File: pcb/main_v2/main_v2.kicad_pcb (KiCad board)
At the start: 4 copper layers, 68.5 x 135.2 mm, 97 parts, among them IC201 AP22811AW5-7, IC301 SE2576L-R, IC302 RMS-30+, IC401 RMS-30+, IC402 HMC374, IC501 SPF5043Z, IC502 PD0922J5050S2HF, IC503 SPF5043Z, J102 Conn_02x06_Odd_Even, J201 USB_A, J301 Conn_Coaxial, J302 Conn_Coaxial, J401 Conn_Coaxial, J402 Conn_Coaxial, SW201 SW_DIP_x01, U201 LT3042xMSE, U501 XMB0220K1-50100G, Y501 ASGTX-P-1.500GHZ-1

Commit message: updarted schematic and simulation
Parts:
- removed C504: 100 pF, Capacitor_SMD:C_0402_1005Metric
- removed C505, C509: 0.1 uF, Capacitor_SMD:C_0603_1608Metric
- removed C506, C507, C508, C510, C511, C512: 100 pF, Capacitor_SMD:C_0603_1608Metric
- removed FL501: LFCN-1700D+, My Footprints:LFCN1700D
- removed IC501, IC503: SPF5043Z, My Footprints:SPF5043Z
- removed IC502: PD0922J5050S2HF, My Footprints:PD0922J5050S2HF
- removed J102: Conn_02x06_Odd_Even, Connector_PinHeader_2.54mm:PinHeader_2x06_P2.54mm_Vertical
- removed L501, L502: 27 nH, Inductor_SMD:L_0603_1608Metric
- removed R501: 10, Resistor_SMD:R_0402_1005Metric
- removed R502, R503: 150 R, Resistor_SMD:R_0603_1608Metric
- removed R504, R505: DNI, Resistor_SMD:R_0603_1608Metric
- removed U501: XMB0220K1-50100G, My Footprints:XMB0220K1-50100G_TTT
- removed Y501: ASGTX-P-1.500GHZ-1, My Footprints:ASGTX
- added C408: 150 pF, Capacitor_SMD:C_0402_1005Metric, F.Cu at (179.9, 148.6)
- added C601: 0.1 uF, Capacitor_SMD:C_0402_1005Metric, F.Cu at (192.0, 124.0)
- added C602: 10 pF, Capacitor_SMD:C_0402_1005Metric, F.Cu at (192.0, 126.0)
- added C603: 0.1 uF, Capacitor_SMD:C_0402_1005Metric, F.Cu at (192.0, 127.9)
- added C604: 10 pF, Capacitor_SMD:C_0402_1005Metric, F.Cu at (192.0, 129.9)
- added C605: 2.7 nF, Capacitor_SMD:C_0402_1005Metric, F.Cu at (192.0, 131.9)
- added C606: 1.2 nF, Capacitor_SMD:C_0402_1005Metric, F.Cu at (192.0, 133.8)
- added C607: 39 nF, Capacitor_SMD:C_0402_1005Metric, F.Cu at (192.0, 135.8)
- added C608: 10 pF, Capacitor_SMD:C_0402_1005Metric, F.Cu at (194.8, 124.0)
- added C609: 0.1 uF, Capacitor_SMD:C_0402_1005Metric, F.Cu at (194.8, 126.0)
- added C610: 0.1 uF, Capacitor_SMD:C_0402_1005Metric, F.Cu at (194.8, 127.9)
- added C611: 120 pF, Capacitor_SMD:C_0402_1005Metric, F.Cu at (194.8, 129.9)
- added C612: 120 pF, Capacitor_SMD:C_0402_1005Metric, F.Cu at (194.8, 131.9)
- added C613: 1 nF, Capacitor_SMD:C_0402_1005Metric, F.Cu at (194.8, 133.8)
- added C614: 1 nF, Capacitor_SMD:C_0402_1005Metric, F.Cu at (194.8, 135.8)
- added C615: 10 pF, Capacitor_SMD:C_0402_1005Metric, F.Cu at (197.7, 124.0)
- added C616: 0.1 uF, Capacitor_SMD:C_0402_1005Metric, F.Cu at (197.7, 126.0)
- added C617: 10 pF, Capacitor_SMD:C_0402_1005Metric, F.Cu at (197.7, 127.9)
- added C618: 0.1 uF, Capacitor_SMD:C_0402_1005Metric, F.Cu at (197.7, 129.9)
- added C619: 10 pF, Capacitor_SMD:C_0402_1005Metric, F.Cu at (197.7, 131.9)
- added C620: 10 pF, Capacitor_SMD:C_0402_1005Metric, F.Cu at (197.7, 133.8)
- added C621: 0.1 uF, Capacitor_SMD:C_0402_1005Metric, F.Cu at (197.7, 135.8)
- added C622: 10 pF, Capacitor_SMD:C_0402_1005Metric, F.Cu at (200.6, 124.0)
- added C623: 0.1 uF, Capacitor_SMD:C_0402_1005Metric, F.Cu at (200.6, 126.0)
- added C624: 1 pF, Capacitor_SMD:C_0402_1005Metric, F.Cu at (200.6, 127.9)
- added C625: 1 pF, Capacitor_SMD:C_0402_1005Metric, F.Cu at (200.6, 129.9)
- added C626: 0.1 uF, Capacitor_SMD:C_0402_1005Metric, F.Cu at (200.6, 131.9)
- added C627: DC Cut Cap, Capacitor_SMD:C_0402_1005Metric, F.Cu at (199.6, 149.1)
- added C628: 10 pF, Capacitor_SMD:C_0402_1005Metric, F.Cu at (199.6, 151.1)
- added C629: 100 pF, Capacitor_SMD:C_0402_1005Metric, F.Cu at (212.3, 134.3)
- added C630: 100 pF, Capacitor_SMD:C_0402_1005Metric, F.Cu at (212.3, 136.2)
- added C631: 10 nF, Capacitor_SMD:C_0402_1005Metric, F.Cu at (212.3, 138.2)
- added C632: 100 pF, Capacitor_SMD:C_0402_1005Metric, F.Cu at (212.3, 140.2)
- added C633: 10 nF, Capacitor_SMD:C_0402_1005Metric, F.Cu at (212.3, 142.1)
- added C634: 100 pF, Capacitor_SMD:C_0402_1005Metric, F.Cu at (212.3, 144.1)
- added D601: LED, LED_SMD:LED_0805_2012Metric, F.Cu at (187.8, 139.6)
- added FL601: LFCN-1800+, My Footprints:LFCN1800, F.Cu at (217.2, 142.2)
- added H101: MountingHole, MountingHole:MountingHole_2.2mm_M2, F.Cu at (78.0, 61.5)
- added H102: MountingHole, MountingHole:MountingHole_2.2mm_M2, F.Cu at (138.0, 61.0)
- added H103: MountingHole, MountingHole:MountingHole_2.2mm_M2, F.Cu at (77.5, 188.0)
- added H104: MountingHole, MountingHole:MountingHole_2.2mm_M2, F.Cu at (137.5, 187.5)
- added IC601: PSA4-5043+, My Footprints:PSA45043, F.Cu at (216.5, 136.4)
- added IC602: PSA4-5043+, My Footprints:PSA45043, F.Cu at (221.9, 136.4)
- added J202: Barrel_Jack, Connector_BarrelJack:BarrelJack_CUI_PJ-063AH_Horizontal_CircularHoles, F.Cu at (132.0, 114.8)
- added L601: 7.5 nH, Inductor_SMD:L_0402_1005Metric, F.Cu at (197.1, 137.8)
- added L602: 7.5 nH, Inductor_SMD:L_0402_1005Metric, F.Cu at (197.1, 139.8)
- added L603: 47 nH, Inductor_SMD:L_0402_1005Metric, F.Cu at (222.0, 140.5)
- added L605: 47 nH, Inductor_SMD:L_0402_1005Metric, F.Cu at (220.0, 127.5)
- added R601: 51, Resistor_SMD:R_0603_1608Metric, F.Cu at (180.5, 124.3)
- added R602: 4.7 k, Resistor_SMD:R_0603_1608Metric, F.Cu at (180.5, 126.8)
- added R603: 360, Resistor_SMD:R_0603_1608Metric, F.Cu at (180.5, 129.3)
- added R604: 680, Resistor_SMD:R_0603_1608Metric, F.Cu at (180.5, 131.8)
- added R605: 10k, Resistor_SMD:R_0603_1608Metric, F.Cu at (180.5, 134.3)
- added R606: 10k, Resistor_SMD:R_0603_1608Metric, F.Cu at (180.5, 136.8)
- added R607: DNI, Resistor_SMD:R_0603_1608Metric, F.Cu at (184.5, 124.3)
- added R608: 10k, Resistor_SMD:R_0603_1608Metric, F.Cu at (184.5, 126.8)
- added R609: 10k, Resistor_SMD:R_0603_1608Metric, F.Cu at (184.5, 129.3)
- added R610: 10k, Resistor_SMD:R_0603_1608Metric, F.Cu at (184.5, 131.8)
- added R611: DNI, Resistor_SMD:R_0603_1608Metric, F.Cu at (184.5, 134.3)
- added R612: 0, Resistor_SMD:R_0603_1608Metric, F.Cu at (184.5, 136.8)
- added R613: 100, Resistor_SMD:R_0603_1608Metric, F.Cu at (188.5, 124.3)
- added R614: 0, Resistor_SMD:R_0603_1608Metric, F.Cu at (188.5, 126.8)
- added R615: 0, Resistor_SMD:R_0603_1608Metric, F.Cu at (188.5, 129.3)
- added R701: 200, Resistor_SMD:R_0402_1005Metric, F.Cu at (198.1, 157.0)
- added R702: 100, Resistor_SMD:R_0402_1005Metric, F.Cu at (198.1, 159.0)
- added U601: ADF4351, Package_CSP:LFCSP-32-1EP_5x5mm_P0.5mm_EP3.25x3.25mm, F.Cu at (182.0, 141.6)
- added U602: XMB0220K1-50100G, My Footprints:XMB0220K1-50100G_TTT, F.Cu at (187.7, 143.1)
- added U701: PD0922J5050D2HF, My Footprints:PD0922J5050D2HF, F.Cu at (194.1, 158.2)
- added Y601: ATX-11-F-26.000MHZ-F05-T, My Footprints:ATX11F26000MHZF05T, F.Cu at (194.8, 151.1)
- C501: value 100 pF -> 0.1 uF
- C502: value 100 pF -> 10 pF
- C503: value 100 pF -> 120 pF
- D202, D203, D204, D205, D301: footprint LED_SMD:LED_0603_1608Metric -> LED_SMD:LED_0805_2012Metric
- moved C501 120.3 mm to (212.3, 148.1)
- moved C503 105.4 mm to (212.3, 152.0)
- moved C502 102.8 mm to (212.3, 150.1), turned to 0 degrees
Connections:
- net /receiver/Rx In renamed /receiver/f = 2.4 GHz
- net /receiver/Rx In 1 renamed Net-(FL401-IN/OUT)
- net /receiver/downconverted Rx renamed Net-(IC401-IF)
- net /receiver/downconverted Rx 1 renamed Net-(FL402-RF_IN)
- net /receiver/lo in renamed Net-(IC401-LO)
- net /receiver/low filtered Rx renamed Net-(FL402-RF_OUT)
- net /receiver/low filtered Rx 1 renamed /receiver/f_sdr = 0.9 GHz
- net /transmitter/LO in renamed Net-(IC302-LO)
- net /transmitter/Power 1 renamed Net-(IC301-VCC1)
- net /transmitter/Tx In 1 renamed Net-(IC302-IF)
- net /transmitter/Upconverted renamed Net-(IC302-RF)
- net /transmitter/Upconverted 1 renamed /transmitter/f_antenne = 2.4 GHz
- net /transmitter/amplified Tx renamed Net-(IC301-RFOUT)
- net /transmitter/amplified Tx 1 renamed Net-(C306-Pad2)
- net /transmitter/amplified Tx 2 renamed Net-(J301-In)
- net CONN-2 renamed /IO Interface/Power Faulty
- net CONN-3 renamed /IO Interface/PA Enable
- net CONN-4 renamed /IO Interface/PA DET Output
- net USB Power renamed /power/USB Power
- C312 pad 2: Carrier Frequency: Tx -> /OX Splitter/Oscillator Tx
- C403 pad 2: Carrier Frequency: Rx -> /OX Splitter/Oscillator Rx
- C404 pad 1: /receiver/amplified Rx -> Net-(IC402-OUT)
- C404 pad 2: /receiver/amplified Rx 1 -> /receiver/amplified Rx
- C501 pad 1: /oscillator/unbalanced OX DC0 -> +3.3V
- C501 pad 2: /oscillator/unbalanced OX 1 -> GND
- C502 pad 1: Net-(Y501-BY-PASS/VC) -> +3.3V
- C503 pad 1: /oscillator/TXC 0DC P -> GND
- C503 pad 2: /oscillator/TCX P -> +3.3V
- FL401 pad 4: /receiver/filtered Rx -> Net-(FL401-_IN/OUT)
- IC401 pad 4: /receiver/amplified Rx 1 -> /receiver/amplified Rx
- IC402 pad 3: /receiver/filtered Rx -> Net-(IC402-IN)
- IC402 pad 6: /receiver/amplified Rx -> Net-(IC402-OUT)
- L401 pad 2: /receiver/amplified Rx -> Net-(IC402-OUT)
- SW201 pad 1: CONN-1 -> /IO Interface/Power Enable
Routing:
- net +5V: track 279.6 -> 160.9 mm, vias 78 -> 52
- net GND: track 368.6 -> 277.3 mm, vias 180 -> 139
- net CONN-1: track 74.9 -> 0.00 mm, vias 2 -> 0
- net /IO Interface/Power Enable: track 0.00 -> 71.4 mm, vias 0 -> 1
- net +3.3V: track 81.9 -> 42.2 mm, vias 37 -> 18
- net /oscillator/TCX P: track 23.9 -> 0.00 mm
- net /oscillator/TCX N: track 20.5 -> 0.00 mm
- net /oscillator/amplified XO 1: track 15.9 -> 0.00 mm
- net Net-(Y501-BY-PASS/VC): track 11.7 -> 0.00 mm
- net /oscillator/filtered XO 1: track 11.6 -> 0.00 mm
- net Net-(IC402-OUT): track 0.00 -> 10.3 mm
- net Carrier Frequency: Tx: track 9.54 -> 0.00 mm
- net /oscillator/amplified XO 2: track 8.90 -> 0.00 mm
- net /oscillator/TXC 0DC N: track 8.54 -> 0.00 mm
- net /oscillator/TXC 0DC P: track 7.65 -> 0.00 mm
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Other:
- board text added: "TODO: - via fencing - via sticthicng with ground plane - component values on silkscreen"
- board text removed: "TODO: - via fencing - via sticthicng with ground plane"

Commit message: improved python mode
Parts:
- removed C205: 4.7 nF, Capacitor_SMD:C_1206_3216Metric
- removed J201: USB_A, Connector_USB:USB3_A_Receptacle_Wuerth_692122030100
- removed J202: Barrel_Jack, Connector_BarrelJack:BarrelJack_CUI_PJ-063AH_Horizontal_CircularHoles
- removed J301, J302, J401, J402: Conn_Coaxial, Connector_Coaxial:SMA_Amphenol_132289_EdgeMount
- removed R202: 1M, Resistor_SMD:R_0603_1608Metric
- added J101: Conn_Coaxial, Connector_Coaxial:SMA_Amphenol_132289_EdgeMount, F.Cu at (242.8, 107.6)
- added J102: Conn_Coaxial, Connector_Coaxial:SMA_Amphenol_132289_EdgeMount, F.Cu at (242.8, 119.8)
- added J103: Conn_Coaxial, Connector_Coaxial:SMA_Amphenol_132289_EdgeMount, F.Cu at (242.8, 132.0)
- added J104: Conn_Coaxial, Connector_Coaxial:SMA_Amphenol_132289_EdgeMount, F.Cu at (242.8, 144.2)
- added J105: Barrel_Jack, Connector_BarrelJack:BarrelJack_CUI_PJ-063AH_Horizontal_CircularHoles, F.Cu at (265.0, 104.5)
- added J701: Conn_01x03_Pin, Connector_PinHeader_2.54mm:PinHeader_1x03_P2.54mm_Vertical, F.Cu at (136.4, 112.3)
- C313, C314, C406, C407: value 10 pF -> 100 pF
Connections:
- net /OX Splitter/Oscillator In renamed Net-(FL601-RF_IN)
- net /OX Splitter/Oscillator Rx renamed /Oscillator Splitter/Oscillator Rx
- net /OX Splitter/Oscillator Tx renamed /Oscillator Splitter/Oscillator Tx
- net /OX Splitter/Rx renamed /Oscillator Splitter/Rx
- net /OX Splitter/Tx renamed /Oscillator Splitter/Tx
- net /oscillator/TCXO renamed /Phase locked loop/TCXO
- net /transmitter/f_antenne = 2.4 GHz renamed Net-(FL301-IN/OUT)
- net Net-(J301-In) renamed /transmitter/Tx Out
- C404 pad 1: Net-(IC402-OUT) -> Net-(IC401-RF)
- C405 pad 1: /receiver/f = 2.4 GHz -> /receiver/Rx In
- C407 pad 2: /receiver/f_sdr = 0.9 GHz -> /receiver/Rx Out
- C624 pad 2: /oscillator/OX Out + -> /Oscillator Splitter/Oscillator In +
- C625 pad 2: /oscillator/OX Out - -> /Oscillator Splitter/Oscillator In -
- C631 pad 1: unconnected-(C631-Pad1) -> GND
- C633 pad 1: unconnected-(C633-Pad1) -> GND
- FL402 pad 1: GND -> unconnected-(FL402-GROUND_1-Pad1)
- IC401 pad 4: /receiver/amplified Rx -> Net-(IC401-RF)
- IC402 pad 6: Net-(IC402-OUT) -> /receiver/amplified Rx
- L401 pad 2: Net-(IC402-OUT) -> /receiver/amplified Rx
- L601 pad 2: /oscillator/OX Out + -> /Oscillator Splitter/Oscillator In +
- L602 pad 2: /oscillator/OX Out - -> /Oscillator Splitter/Oscillator In -
- U602 pad 5: /oscillator/OX Out - -> /Oscillator Splitter/Oscillator In +
- U602 pad 6: /oscillator/OX Out + -> /Oscillator Splitter/Oscillator In -
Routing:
- net /power/Shield: track 37.8 -> 0.00 mm
- net (no net): track 7.35 -> 45.2 mm
- net /receiver/f_sdr = 0.9 GHz: track 12.6 -> 0.00 mm
- net /receiver/Rx Out: track 0.00 -> 12.6 mm
- net /receiver/f = 2.4 GHz: track 10.9 -> 0.00 mm
- net /receiver/Rx In: track 0.00 -> 10.9 mm
- net Net-(IC402-OUT): track 10.3 -> 0.00 mm
- net /receiver/amplified Rx: track 5.58 -> 15.9 mm
- net GND: track 277.3 -> 273.1 mm, vias 139 -> 137
- net unconnected-(FL402-GROUND_1-Pad1): track 0.00 -> 4.21 mm, vias 0 -> 2

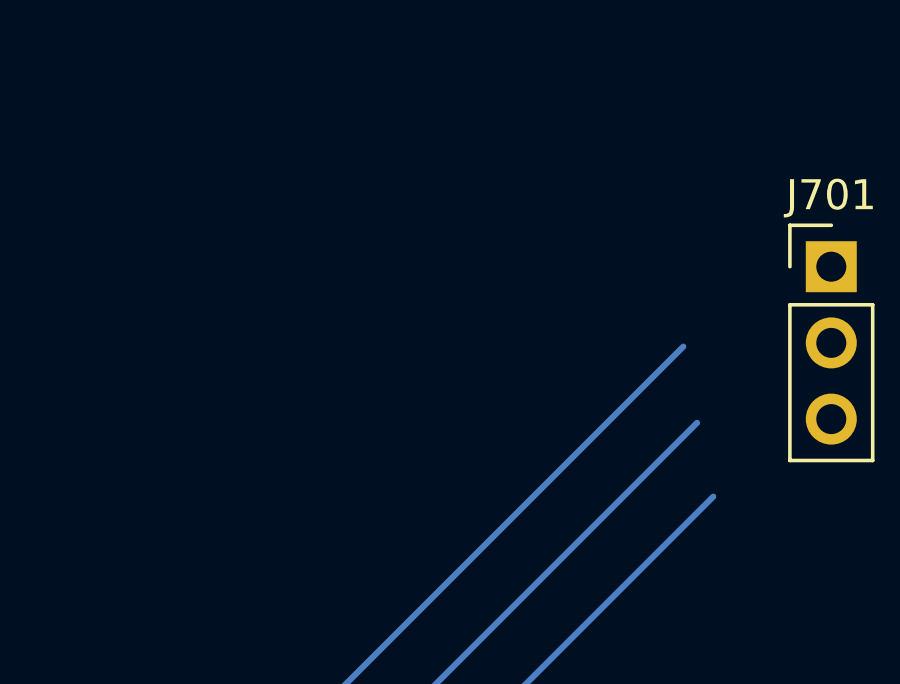
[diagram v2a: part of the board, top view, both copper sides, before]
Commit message: added noise calc for simulation
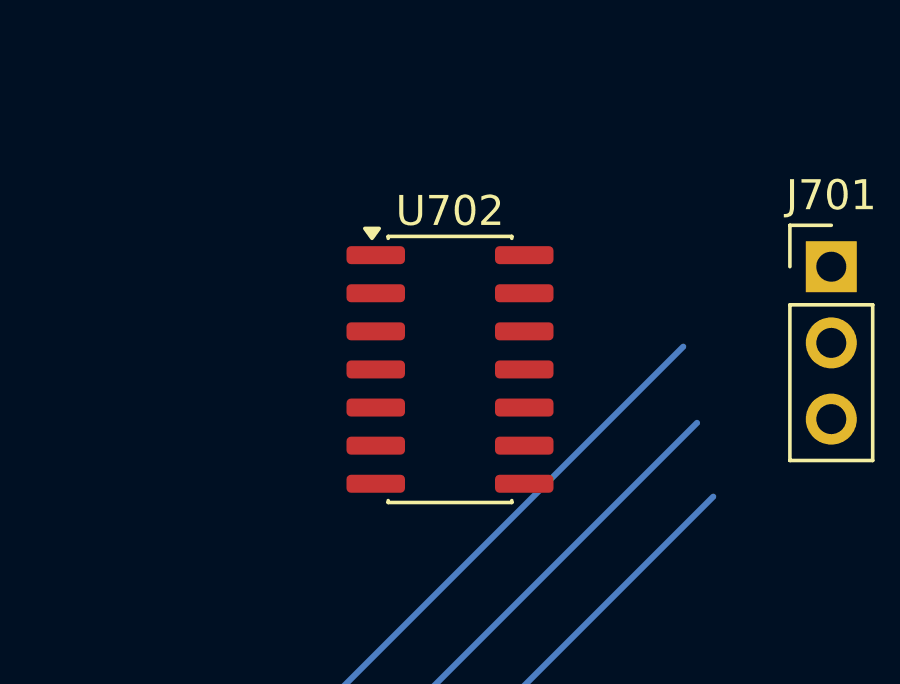
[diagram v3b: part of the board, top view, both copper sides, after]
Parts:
- added U702: TXB0104D, Package_SO:SOIC-14_3.9x8.7mm_P1.27mm, F.Cu at (123.7, 115.8)

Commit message: updated io schematic
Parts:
- removed C314, C629, C630, C632, C634: 100 pF, Capacitor_SMD:C_0402_1005Metric
- removed C607: 39 nF, Capacitor_SMD:C_0402_1005Metric
- removed C608, C615, C617, C619, C620, C622, C628: 10 pF, Capacitor_SMD:C_0402_1005Metric
- removed C609, C610, C616, C618, C621, C623, C626: 0.1 uF, Capacitor_SMD:C_0402_1005Metric
- removed C611, C612: 120 pF, Capacitor_SMD:C_0402_1005Metric
- removed C613, C614: 1 nF, Capacitor_SMD:C_0402_1005Metric
- removed C624, C625: 1 pF, Capacitor_SMD:C_0402_1005Metric
- removed C627: DC Cut Cap, Capacitor_SMD:C_0402_1005Metric
- removed C631, C633: 10 nF, Capacitor_SMD:C_0402_1005Metric
- removed D601: LED, LED_SMD:LED_0805_2012Metric
- removed L603, L605: 47 nH, Inductor_SMD:L_0402_1005Metric
- removed R206: 453 k, Resistor_SMD:R_0603_1608Metric
- removed R603: 360, Resistor_SMD:R_0603_1608Metric
- removed R604: 680, Resistor_SMD:R_0603_1608Metric
- removed R605, R606, R608, R609, R610: 10k, Resistor_SMD:R_0603_1608Metric
- removed R607, R611: DNI, Resistor_SMD:R_0603_1608Metric
- removed R612, R614, R615: 0, Resistor_SMD:R_0603_1608Metric
- removed R613: 100, Resistor_SMD:R_0603_1608Metric
- removed U701: PD0922J5050D2HF, My Footprints:PD0922J5050D2HF
- removed U702: TXB0104D, Package_SO:SOIC-14_3.9x8.7mm_P1.27mm
- removed Y601: ATX-11-F-26.000MHZ-F05-T, My Footprints:ATX11F26000MHZF05T
- added C205: 4.7 uF, Capacitor_SMD:C_0603_1608Metric, F.Cu at (382.7, 108.1)
- added C311: 10 pF, Capacitor_SMD:C_0402_1005Metric, F.Cu at (388.1, 107.8)
- added C504: 0.1 uF, Capacitor_SMD:C_0402_1005Metric, F.Cu at (382.1, 83.7)
- added C505: 10 pF, Capacitor_SMD:C_0402_1005Metric, F.Cu at (382.1, 85.7)
- added C506: 0.1 uF, Capacitor_SMD:C_0402_1005Metric, F.Cu at (382.1, 87.6)
- added C507: 10 pF, Capacitor_SMD:C_0402_1005Metric, F.Cu at (382.1, 89.6)
- added C508: 10 pF, Capacitor_SMD:C_0402_1005Metric, F.Cu at (382.1, 91.6)
- added C509: 0.1 uF, Capacitor_SMD:C_0402_1005Metric, F.Cu at (382.1, 93.5)
- added C510: 120 pF, Capacitor_SMD:C_0402_1005Metric, F.Cu at (382.1, 95.5)
- added C511: 10 pF, Capacitor_SMD:C_0402_1005Metric, F.Cu at (382.1, 97.5)
- added C512: 0.1 uF, Capacitor_SMD:C_0402_1005Metric, F.Cu at (385.0, 83.7)
- added C513: 120 pF, Capacitor_SMD:C_0402_1005Metric, F.Cu at (385.0, 85.7)
- added C514: 1 pF, Capacitor_SMD:C_0402_1005Metric, F.Cu at (385.0, 87.6)
- added C515: 1 pF, Capacitor_SMD:C_0402_1005Metric, F.Cu at (385.0, 89.6)
- added C516: 1 nF, Capacitor_SMD:C_0402_1005Metric, F.Cu at (385.0, 91.6)
- added C517: 1 nF, Capacitor_SMD:C_0402_1005Metric, F.Cu at (385.0, 93.5)
- added C518: 0.1 uF, Capacitor_SMD:C_0402_1005Metric, F.Cu at (385.0, 95.5)
- added C519: 10 pF, Capacitor_SMD:C_0402_1005Metric, F.Cu at (385.0, 97.5)
- added C520: 2.7 nF, Capacitor_SMD:C_0402_1005Metric, F.Cu at (387.9, 83.7)
- added C521: 39 nF, Capacitor_SMD:C_0402_1005Metric, F.Cu at (387.9, 85.7)
- added C522: 1.2 nF, Capacitor_SMD:C_0402_1005Metric, F.Cu at (387.9, 87.6)
- added C523: 0.1 uF, Capacitor_SMD:C_0402_1005Metric, F.Cu at (387.9, 89.6)
- added C524: 10 pF, Capacitor_SMD:C_0402_1005Metric, F.Cu at (387.9, 91.6)
- added C525: 0.1 uF, Capacitor_SMD:C_0402_1005Metric, F.Cu at (387.9, 93.5)
- added C526: 10 pF, Capacitor_SMD:C_0402_1005Metric, F.Cu at (387.9, 95.5)
- added C527: DC Cut Cap, Capacitor_SMD:C_0402_1005Metric, F.Cu at (387.9, 97.5)
- added C528: 120 pF, Capacitor_SMD:C_0402_1005Metric, F.Cu at (390.7, 83.7)
- added C529: 0.1 uF, Capacitor_SMD:C_0402_1005Metric, F.Cu at (390.7, 85.7)
- added C530: 10 pF, Capacitor_SMD:C_0402_1005Metric, F.Cu at (390.7, 87.6)
- added C531: 10 pF, Capacitor_SMD:C_0402_1005Metric, F.Cu at (390.7, 89.6)
- added C701: 0.1 uF, Capacitor_SMD:C_0402_1005Metric, F.Cu at (378.1, 55.7)
- added C702: 0.1 uF, Capacitor_SMD:C_0402_1005Metric, F.Cu at (378.1, 57.7)
- added C703: 0.1 uF, Capacitor_SMD:C_0402_1005Metric, F.Cu at (102.7, 128.7)
- added D206: LED, LED_SMD:LED_0805_2012Metric, F.Cu at (136.6, 122.3)
- added D501: LED, LED_SMD:LED_0805_2012Metric, F.Cu at (389.6, 100.0)
- added FB201: 28C0236-0JW-10, Ferrite_THT:LairdTech_28C0236-0JW-10, F.Cu at (127.3, 113.2)
- added FB202: 28C0236-0JW-10, Ferrite_THT:LairdTech_28C0236-0JW-10, F.Cu at (127.3, 122.1)
- added IC701: 74LVC244AD-Q100J, My Footprints:SOIC127P1032X265-20N, F.Cu at (107.7, 116.0)
- added IC702: LTC6992CS6-4#TRMPBF, My Footprints:SOT95P280X100-6N, F.Cu at (103.8, 125.5)
- added J702: Conn_01x01_Pin, Connector_PinHeader_2.54mm:PinHeader_1x01_P2.54mm_Vertical, F.Cu at (140.1, 70.5)
- added J703: Conn_01x03_Pin, Connector_PinHeader_2.54mm:PinHeader_1x03_P2.54mm_Vertical, F.Cu at (94.6, 79.0)
- added J704: Conn_01x03_Pin, Connector_PinHeader_2.54mm:PinHeader_1x03_P2.54mm_Vertical, F.Cu at (147.6, 70.4)
- added J705: Conn_01x01_Pin, Connector_PinHeader_2.54mm:PinHeader_1x01_P2.54mm_Vertical, F.Cu at (143.9, 70.5)
- added J706: Conn_01x01_Pin, Connector_PinHeader_2.54mm:PinHeader_1x01_P2.54mm_Vertical, F.Cu at (112.6, 78.0)
- added J707: Conn_01x01_Pin, Connector_PinHeader_2.54mm:PinHeader_1x01_P2.54mm_Vertical, F.Cu at (108.6, 78.0)
- added J709: Conn_01x03_Pin, Connector_PinHeader_2.54mm:PinHeader_1x03_P2.54mm_Vertical, F.Cu at (116.5, 123.6)
- added J710: Conn_01x03_Pin, Connector_PinHeader_2.54mm:PinHeader_1x03_P2.54mm_Vertical, F.Cu at (121.1, 123.6)
- added L501: 7.5 nH, Inductor_SMD:L_0402_1005Metric, F.Cu at (400.7, 98.8)
- added L502: 7.5 nH, Inductor_SMD:L_0402_1005Metric, F.Cu at (400.7, 100.8)
- added Q201: DMP3068L-7, My Footprints:SOT96P240X115-3N, F.Cu at (136.8, 118.6)
- added R202: 1k, Resistor_SMD:R_0603_1608Metric, F.Cu at (382.7, 110.6)
- added R212: 1k, Resistor_SMD:R_0603_1608Metric, F.Cu at (136.3, 115.0)
- added R501: 100, Resistor_SMD:R_0603_1608Metric, F.Cu at (394.2, 84.0)
- added R502: 10k, Resistor_SMD:R_0603_1608Metric, F.Cu at (394.2, 86.5)
- added R503: 10k, Resistor_SMD:R_0603_1608Metric, F.Cu at (394.2, 89.0)
- added R504: 10k, Resistor_SMD:R_0603_1608Metric, F.Cu at (394.2, 91.5)
- added R505: DNI, Resistor_SMD:R_0603_1608Metric, F.Cu at (394.2, 94.0)
- added R506: 10k, Resistor_SMD:R_0603_1608Metric, F.Cu at (394.2, 96.5)
- added R507: 0, Resistor_SMD:R_0603_1608Metric, F.Cu at (398.2, 84.0)
- added R508: 0, Resistor_SMD:R_0603_1608Metric, F.Cu at (398.2, 86.5)
- added R509: DNI, Resistor_SMD:R_0603_1608Metric, F.Cu at (398.2, 89.0)
- added R510: 0, Resistor_SMD:R_0603_1608Metric, F.Cu at (398.2, 91.5)
- added R511: 51, Resistor_SMD:R_0603_1608Metric, F.Cu at (398.2, 94.0)
- added R512: 680, Resistor_SMD:R_0603_1608Metric, F.Cu at (398.2, 96.5)
- added R513: 360, Resistor_SMD:R_0603_1608Metric, F.Cu at (402.2, 84.0)
- added R514: 4.7 k, Resistor_SMD:R_0603_1608Metric, F.Cu at (402.2, 86.5)
- added R515: 10k, Resistor_SMD:R_0603_1608Metric, F.Cu at (402.2, 89.0)
- added R703: 100R, Resistor_SMD:R_0603_1608Metric, F.Cu at (140.6, 90.2)
- added R704: 100R, Resistor_SMD:R_0603_1608Metric, F.Cu at (374.7, 58.5)
- added R705: 100R, Resistor_SMD:R_0603_1608Metric, F.Cu at (374.7, 61.0)
- added R706: 100R, Resistor_SMD:R_0603_1608Metric, F.Cu at (374.7, 63.5)
- added R707: 100R, Resistor_SMD:R_0603_1608Metric, F.Cu at (374.7, 66.0)
- added R708: 50k, Resistor_SMD:R_0603_1608Metric, F.Cu at (116.2, 110.0)
- added R709: 100R, Resistor_SMD:R_0603_1608Metric, F.Cu at (116.2, 112.5)
- added R710: 100R, Resistor_SMD:R_0603_1608Metric, F.Cu at (116.2, 115.0)
- added R711: 100R, Resistor_SMD:R_0603_1608Metric, F.Cu at (116.2, 117.5)
- added R712: 100R, Resistor_SMD:R_0603_1608Metric, F.Cu at (116.2, 120.0)
- added U501: ADF4351, Package_CSP:LFCSP-32-1EP_5x5mm_P0.5mm_EP3.25x3.25mm, F.Cu at (395.7, 101.3)
- added U703: TXB0104D, Package_SO:SOIC-14_3.9x8.7mm_P1.27mm, F.Cu at (380.2, 62.5)
- added Y501: ATX-11-F-26.000MHZ-F05-T, My Footprints:ATX11F26000MHZF05T, F.Cu at (384.0, 101.4)
- C208: value 4.7 uF -> 470u
- C312, C602: value 10 pF -> 100 pF
- C403: value 10 pF -> 150 pF
- C405: value 150 pF -> 100 pF
- C406: value 100 pF -> 10 pF
- C503: value 120 pF -> 0.1 uF
- C601: value 0.1 uF -> 10 nF
- C603: value 0.1 uF -> 100 pF
- C604: value 10 pF -> 10 nF
- C605: value 2.7 nF -> 100 pF
- C606: value 1.2 nF -> 100 pF
- IC401: value RMS-30+ -> HMC374; footprint My Footprints:RMS30 -> My Footprints:SOT95P280X145-6N
- IC402: value HMC374 -> RMS-30+; footprint My Footprints:SOT95P280X145-6N -> My Footprints:RMS30
- L601, L602: value 7.5 nH -> 47 nH
- R203: value 1k -> 10k
- R204: value 10k -> 1k
- R205: value 1k -> 453 k
- R207: value 200k -> 499
- R208: value 499 -> 49.9 k
- R209: value 49.9 k -> 150
- R210: value 150 -> 33.2k
- R211: value 33.2k -> 100k
- R601: value 51 -> 100; footprint Resistor_SMD:R_0603_1608Metric -> Resistor_SMD:R_0402_1005Metric
- R602: value 4.7 k -> 200; footprint Resistor_SMD:R_0603_1608Metric -> Resistor_SMD:R_0402_1005Metric
- R701: value 200 -> 100R; footprint Resistor_SMD:R_0402_1005Metric -> Resistor_SMD:R_0603_1608Metric
- R702: value 100 -> 100R; footprint Resistor_SMD:R_0402_1005Metric -> Resistor_SMD:R_0603_1608Metric
- U601: value ADF4351 -> PD0922J5050D2HF; footprint Package_CSP:LFCSP-32-1EP_5x5mm_P0.5mm_EP3.25x3.25mm -> My Footprints:PD0922J5050D2HF
- moved R601 271.0 mm to (451.2, 135.7), turned to -90 degrees
- moved R602 268.4 mm to (448.7, 135.7), turned to -90 degrees
- moved C601 260.6 mm to (451.5, 147.2), turned to -90 degrees
- moved R701 259.6 mm to (446.8, 82.4)
- moved R702 259.6 mm to (446.8, 84.3)
- moved C602 258.4 mm to (449.5, 147.2), turned to -90 degrees
- moved C603 256.3 mm to (447.6, 147.2), turned to -90 degrees
- moved C604 254.2 mm to (445.6, 147.2), turned to -90 degrees
- moved C605 252.1 mm to (443.6, 147.2), turned to -90 degrees
- moved U601 251.9 mm to (433.9, 137.3), turned to -90 degrees
- moved C606 250.0 mm to (441.6, 147.2), turned to -90 degrees
- moved C408 247.3 mm to (426.9, 135.2), turned to -90 degrees
- moved U602 244.7 mm to (432.3, 142.9), turned to -90 degrees
- moved L601 241.0 mm to (437.7, 152.4), turned to -90 degrees
- moved L602 238.9 mm to (435.7, 152.4), turned to -90 degrees
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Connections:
- C206 pad 1: GND -> +5V
- C206 pad 2: +3.3V -> GND
- C207 pad 1: +5V -> Net-(U201-SET)
- C208 pad 1: Net-(U201-SET) -> /power/USB Power
- C312 pad 1: Net-(IC302-LO) -> /transmitter/Tx In
- C312 pad 2: /Oscillator Splitter/Oscillator Tx -> Net-(IC302-IF)
- C313 pad 1: /transmitter/Tx In -> Net-(IC302-RF)
- C313 pad 2: Net-(IC302-IF) -> Net-(FL301-IN/OUT)
- C403 pad 1: Net-(IC401-LO) -> /receiver/Rx In
- C403 pad 2: /Oscillator Splitter/Oscillator Rx -> Net-(FL401-IN/OUT)
- C404 pad 1: Net-(IC401-RF) -> Net-(FL401-_IN/OUT)
- C404 pad 2: /receiver/amplified Rx -> Net-(IC401-IN)
- C405 pad 1: /receiver/Rx In -> Net-(FL402-RF_OUT)
- C405 pad 2: Net-(FL401-IN/OUT) -> /receiver/Rx Out
- C406 pad 1: Net-(IC401-IF) -> Net-(IC402-LO)
- C406 pad 2: Net-(FL402-RF_IN) -> /Oscillator Splitter/Oscillator Rx
- C407 pad 1: Net-(FL402-RF_OUT) -> Net-(IC402-IF)
- C407 pad 2: /receiver/Rx Out -> Net-(FL402-RF_IN)
- C408 pad 1: Net-(FL401-_IN/OUT) -> Net-(IC402-RF)
- C408 pad 2: Net-(IC402-IN) -> /receiver/amplified Rx
- C503 pad 1: GND -> +3.3V
- C503 pad 2: +3.3V -> GND
- C601 pad 1: +3.3V -> GND
- C601 pad 2: GND -> +5V
- C602 pad 1: +3.3V -> Net-(IC601-RF-OUT_&_DC-IN)
- C602 pad 2: GND -> /Oscillator Splitter/Oscillator Tx
- C603 pad 1: +3.3V -> /Oscillator Splitter/Tx
- C603 pad 2: GND -> Net-(IC601-RF_IN)
- C604 pad 1: +3.3V -> GND
- C604 pad 2: GND -> +5V
- C605 pad 1: GND -> Net-(IC602-RF-OUT_&_DC-IN)
- C605 pad 2: Net-(U601-CPout) -> /Oscillator Splitter/Oscillator Rx
- C606 pad 1: GND -> /Oscillator Splitter/Rx
- C606 pad 2: Net-(U601-VTUNE) -> Net-(IC602-RF_IN)
- D201 pad 1: /power/USB Power -> /power/DC Power
- IC201 pad 3: /IO Interface/Power Faulty -> /power/Power Faulty
- IC401 pad 1: Net-(IC401-LO) -> unconnected-(IC401-N/C_1-Pad1)
- IC401 pad 3: GND -> Net-(IC401-IN)
- IC401 pad 4: Net-(IC401-RF) -> unconnected-(IC401-N/C_2-Pad4)
- IC401 pad 5: Net-(IC401-IF) -> GND
- IC401 pad 6: GND -> /receiver/amplified Rx
- IC402 pad 1: unconnected-(IC402-N/C_1-Pad1) -> Net-(IC402-LO)
- IC402 pad 3: Net-(IC402-IN) -> GND
- IC402 pad 4: unconnected-(IC402-N/C_2-Pad4) -> Net-(IC402-RF)
- IC402 pad 5: GND -> Net-(IC402-IF)
- IC402 pad 6: /receiver/amplified Rx -> GND
- J101 pad 1: /receiver/Rx In -> /receiver/Rx Out
- J102 pad 1: /receiver/Rx Out -> /transmitter/Tx Out
- J103 pad 1: /transmitter/Tx In -> /receiver/Rx In
- J104 pad 1: /transmitter/Tx Out -> /transmitter/Tx In
- J105 pad 1: /power/USB Power -> /power/DC Power
- J701 pad 1: /IO Interface/SPI: CLK -> +3.3V
- J701 pad 2: /IO Interface/SPI: DATA -> Net-(IC701-1A0)
- J701 pad 3: /IO Interface/SPI: Load Enable -> GND
- L601 pad 1: +3.3V -> +5V
- L601 pad 2: /Oscillator Splitter/Oscillator In + -> Net-(IC601-RF-OUT_&_DC-IN)
- L602 pad 1: +3.3V -> +5V
- L602 pad 2: /Oscillator Splitter/Oscillator In - -> Net-(IC602-RF-OUT_&_DC-IN)
- R203 pad 1: Net-(D203-K) -> /power/USB Power
- R203 pad 2: GND -> /power/Power Faulty
- R204 pad 1: /power/USB Power -> Net-(D204-K)
- R204 pad 2: /IO Interface/Power Faulty -> /power/Power Faulty
- R205 pad 1: Net-(D204-K) -> Net-(U201-PGFB)
- R205 pad 2: /IO Interface/Power Faulty -> +3.3V
- R207 pad 1: +5V -> GND
- R207 pad 2: Net-(U201-PG) -> Net-(U201-ILIM)
- R208 pad 2: Net-(U201-ILIM) -> Net-(U201-PGFB)
- R209 pad 1: GND -> Net-(D205-K)
- R209 pad 2: Net-(U201-PGFB) -> GND
- R210 pad 1: Net-(D205-K) -> GND
- R210 pad 2: GND -> Net-(U201-SET)
- R211 pad 1: GND -> Net-(Q201-G)
- R211 pad 2: Net-(U201-SET) -> GND
- R601 pad 1: GND -> Net-(U601-MID_1)
- R601 pad 2: Net-(C613-Pad1) -> Net-(U601-MID_2)
- R602 pad 1: GND -> /Oscillator Splitter/Rx
- R602 pad 2: Net-(U601-RSET) -> /Oscillator Splitter/Tx
- R701 pad 1: /Oscillator Splitter/Rx -> /IO Interface/Power Enable
- R701 pad 2: /Oscillator Splitter/Tx -> Net-(IC701-1Y0)
- R702 pad 1: Net-(U701-MID_1) -> /IO Interface/PLL: Power Down
- TP201 pad 1: /power/USB Power -> /power/DC Power
- U201 pad 4: Net-(U201-PG) -> Net-(D206-K)
- U601 pad 1: /IO Interface/SPI: CLK -> /Oscillator Splitter/Tx
- U601 pad 2: /IO Interface/SPI: DATA -> Net-(FL601-RF_OUT)
- U601 pad 3: /IO Interface/SPI: Load Enable -> Net-(U601-MID_2)
- U601 pad 4: /IO Interface/PLL: Chip Enable -> Net-(U601-MID_1)
- U601 pad 5: unconnected-(U601-SW-Pad5) -> GND
- U601 pad 6: +3.3V -> /Oscillator Splitter/Rx
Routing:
- net /IO Interface/Power Faulty: track 78.9 -> 0.00 mm, vias 1 -> 0
- net /IO Interface/Power Enable: track 71.4 -> 30.1 mm
- net (no net): track 45.2 -> 20.5 mm, vias 0 -> 5
- net /power/Power Faulty: track 0.00 -> 23.5 mm, vias 0 -> 3
- net /IO Interface/PA Enable: track 48.6 -> 32.6 mm
- net Net-(FL402-RF_IN): track 23.4 -> 36.0 mm
- net /receiver/Rx Out: track 12.6 -> 0.00 mm
- net +3.3V: track 42.2 -> 30.4 mm, vias 18 -> 13
- net Net-(U201-PG): track 10.3 -> 0.00 mm
- net Net-(U201-ILIM): track 6.76 -> 17.0 mm
- net GND: track 273.1 -> 281.9 mm, vias 137 -> 127
- net Net-(IC401-IF): track 8.73 -> 0.00 mm
- net Net-(IC302-RF): track 4.76 -> 13.0 mm
- net /transmitter/Tx In: track 8.28 -> 0.00 mm
- net Net-(FL401-_IN/OUT): track 0.00 -> 7.35 mm
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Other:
- board size 68.5 x 135.2 mm -> 179.2 x 68.5 mm
- board text added: "Digital In"
- board text added: "Digital Out"
- board text added: "High"
- board text added: "Low"
- board text added: "PA Enable"
- board text added: "PLL Chip Enable"
- board text added: "PLL Lock Detect"
- board text added: "PLL MUXOUT"
- board text added: "PLL Power Down"
- board text added: "PLL: Lock Detect"
- board text added: "Power 3.3V"
- board text added: "Power 5V"
- board text added: "Power Enable"
- board text added: "Power Faulty"
- board text added: "Power: Center +5V"
- board text added: "SDR Frontend Rev 1, 2026 Jan Hoegen hoja1028@h-ka.de"
- board text added: "SPI: Data Clock Enable"
- board text added: "Tx: In -> 0.9 - 1 GHz"
- board text added: "Tx: Out -> 2.4 - 2.5 GHz"
- board text removed: "Rev 1, 2026 Jan Hoegen hoja1028@h-ka.de"
- board text removed: "Tx: In ->"
- board text removed: "Tx: Out ->"
